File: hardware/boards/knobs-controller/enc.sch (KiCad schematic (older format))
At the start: 11 parts, among them SW1 Rotary Encoder

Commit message: 1.8 work-in-progress
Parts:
- C7, C8: footprint footprints:C0805 -> Capacitor_SMD:C_0805_2012Metric
- R10, R11, R12, R13, R14, R15, R8, R9: footprint footprints:R0805 -> Resistor_SMD:R_0805_2012Metric
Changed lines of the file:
@@
 $Descr A4 11693 8268
 encoding utf-8
-Sheet 3 13
+Sheet 5 13
 Title ""
 Date ""
@@
 AR Path="/5D86641C/5D8716A9/5D98B23E" Ref="SW3"  Part="1"
 AR Path="/5D86641C/5D87B0CB/5D98B23E" Ref="SW?"  Part="1"
-F 0 "SW1" H 5500 4570 70  0000 L BNN
+F 0 "SW3" H 5500 4570 70  0000 L BNN
 F 1 "Rotary Encoder" H 5500 3655 70  0000 L BNN
 F 2 "footprints:ENCODER_LED_3_KIT" H 6000 4150 50  0001 C CNN
@@
 AR Path="/5D86641C/5D8716A9/5D98B244" Ref="R28"  Part="1"
 AR Path="/5D86641C/5D87B0CB/5D98B244" Ref="R?"  Part="1"
-F 0 "R12" H 6850 5059 59  0000 L BNN
+F 0 "R28" H 6850 5059 59  0000 L BNN
 F 1 "10k" H 6850 4870 59  0000 L BNN
-F 2 "footprints:R0805" H 7000 5000 50  0001 C CNN
+F 2 "Resistor_SMD:R_0805_2012Metric" H 7000 5000 50  0001 C CNN
 F 3 "" H 7000 5000 50  0001 C CNN
 	1    7000 5000
@@
 AR Path="/5D86641C/5D8716A9/5D98B24A" Ref="R25"  Part="1"
 AR Path="/5D86641C/5D87B0CB/5D98B24A" Ref="R?"  Part="1"
-F 0 "R9" H 4050 3709 59  0000 L BNN
+F 0 "R25" H 4050 3709 59  0000 L BNN
 F 1 "10k" H 4050 3520 59  0000 L BNN
-F 2 "footprints:R0805" H 4200 3650 50  0001 C CNN
+F 2 "Resistor_SMD:R_0805_2012Metric" H 4200 3650 50  0001 C CNN
 F 3 "" H 4200 3650 50  0001 C CNN
 	1    4200 3650
@@
 AR Path="/5D86641C/5D8716A9/5D98B250" Ref="R24"  Part="1"
 AR Path="/5D86641C/5D87B0CB/5D98B250" Ref="R?"  Part="1"
-F 0 "R8" H 3750 4009 59  0000 L BNN
+F 0 "R24" H 3750 4009 59  0000 L BNN
 F 1 "10k" H 3750 3820 59  0000 L BNN
-F 2 "footprints:R0805" H 3900 3950 50  0001 C CNN
+F 2 "Resistor_SMD:R_0805_2012Metric" H 3900 3950 50  0001 C CNN
 F 3 "" H 3900 3950 50  0001 C CNN
 	1    3900 3950
@@
 AR Path="/5D86641C/5D8716A9/5D98B256" Ref="R27"  Part="1"
 AR Path="/5D86641C/5D87B0CB/5D98B256" Ref="R?"  Part="1"
-F 0 "R11" H 5050 3709 59  0000 L BNN
+F 0 "R27" H 5050 3709 59  0000 L BNN
 F 1 "10k" H 5050 3520 59  0000 L BNN
-F 2 "footprints:R0805" H 5200 3650 50  0001 C CNN
+F 2 "Resistor_SMD:R_0805_2012Metric" H 5200 3650 50  0001 C CNN
 F 3 "" H 5200 3650 50  0001 C CNN
 	1    5200 3650
@@
 AR Path="/5D86641C/5D8716A9/5D98B25C" Ref="R26"  Part="1"
 AR Path="/5D86641C/5D87B0CB/5D98B25C" Ref="R?"  Part="1"
-F 0 "R10" H 4750 4409 59  0000 L BNN
+F 0 "R26" H 4750 4409 59  0000 L BNN
 F 1 "10k" H 4750 4220 59  0000 L BNN
-F 2 "footprints:R0805" H 4900 4350 50  0001 C CNN
+F 2 "Resistor_SMD:R_0805_2012Metric" H 4900 4350 50  0001 C CNN
 F 3 "" H 4900 4350 50  0001 C CNN
 	1    4900 4350
@@
 AR Path="/5D86641C/5D8716A9/5D98B262" Ref="C12"  Part="1"
 AR Path="/5D86641C/5D87B0CB/5D98B262" Ref="C?"  Part="1"
-F 0 "C8" H 4660 4765 59  0000 L BNN
+F 0 "C12" H 4660 4765 59  0000 L BNN
 F 1 "10nF" H 4660 4465 59  0001 L BNN
-F 2 "footprints:C0805" H 4600 4650 50  0001 C CNN
+F 2 "Capacitor_SMD:C_0805_2012Metric" H 4600 4650 50  0001 C CNN
 F 3 "" H 4600 4650 50  0001 C CNN
 	1    4600 4650
@@
 AR Path="/5D86641C/5D8716A9/5D98B268" Ref="C11"  Part="1"
 AR Path="/5D86641C/5D87B0CB/5D98B268" Ref="C?"  Part="1"
-F 0 "C7" H 3660 4265 59  0000 L BNN
+F 0 "C11" H 3660 4265 59  0000 L BNN
 F 1 "10nF" H 3660 4065 59  0000 L BNN
-F 2 "footprints:C0805" H 3600 4250 50  0001 C CNN
+F 2 "Capacitor_SMD:C_0805_2012Metric" H 3600 4250 50  0001 C CNN
 F 3 "" H 3600 4250 50  0001 C CNN
 	1    3600 4250
@@
 AR Path="/5D86641C/5D8716A9/5D98B26E" Ref="R29"  Part="1"
 AR Path="/5D86641C/5D87B0CB/5D98B26E" Ref="R?"  Part="1"
-F 0 "R13" H 7050 3909 59  0000 L BNN
+F 0 "R29" H 7050 3909 59  0000 L BNN
 F 1 "10" H 7050 3720 59  0000 L BNN
-F 2 "footprints:R0805" H 7200 3850 50  0001 C CNN
+F 2 "Resistor_SMD:R_0805_2012Metric" H 7200 3850 50  0001 C CNN
 F 3 "" H 7200 3850 50  0001 C CNN
 	1    7200 3850
@@
 AR Path="/5D86641C/5D8716A9/5D98B274" Ref="R30"  Part="1"
 AR Path="/5D86641C/5D87B0CB/5D98B274" Ref="R?"  Part="1"
-F 0 "R14" H 7050 4209 59  0000 L BNN
+F 0 "R30" H 7050 4209 59  0000 L BNN
 F 1 "10" H 7050 4020 59  0000 L BNN
-F 2 "footprints:R0805" H 7200 4150 50  0001 C CNN
+F 2 "Resistor_SMD:R_0805_2012Metric" H 7200 4150 50  0001 C CNN
 F 3 "" H 7200 4150 50  0001 C CNN
 	1    7200 4150
@@
 AR Path="/5D86641C/5D8716A9/5D98B27A" Ref="R31"  Part="1"
 AR Path="/5D86641C/5D87B0CB/5D98B27A" Ref="R?"  Part="1"
-F 0 "R15" H 7050 4509 59  0000 L BNN
+F 0 "R31" H 7050 4509 59  0000 L BNN
 F 1 "10" H 7050 4320 59  0000 L BNN
-F 2 "footprints:R0805" H 7200 4450 50  0001 C CNN
+F 2 "Resistor_SMD:R_0805_2012Metric" H 7200 4450 50  0001 C CNN
 F 3 "" H 7200 4450 50  0001 C CNN
 	1    7200 4450
@@
 AR Path="/5D86641C/5D8716A9/5D98B281" Ref="#+3V010"  Part="1"
 AR Path="/5D86641C/5D87B0CB/5D98B281" Ref="#+3V?"  Part="1"
-F 0 "#+3V04" H 5200 3250 50  0001 C CNN
+F 0 "#+3V010" H 5200 3250 50  0001 C CNN
 F 1 "+3V3" H 5200 3372 59  0000 C CNN
 F 2 "" H 5200 3250 50  0001 C CNN
@@
 AR Path="/5D86641C/5D8716A9/5D98B287" Ref="#GND016"  Part="1"
 AR Path="/5D86641C/5D87B0CB/5D98B287" Ref="#GND?"  Part="1"
-F 0 "#GND08" H 4600 4950 50  0001 C CNN
+F 0 "#GND016" H 4600 4950 50  0001 C CNN
 F 1 "GND" H 4600 4829 59  0000 C CNN
 F 2 "" H 4600 4950 50  0001 C CNN
@@
 AR Path="/5D86641C/5D8716A9/5D98B28D" Ref="#+3V09"  Part="1"
 AR Path="/5D86641C/5D87B0CB/5D98B28D" Ref="#+3V?"  Part="1"
-F 0 "#+3V03" H 4200 3250 50  0001 C CNN
+F 0 "#+3V09" H 4200 3250 50  0001 C CNN
 F 1 "+3V3" H 4200 3372 59  0000 C CNN
 F 2 "" H 4200 3250 50  0001 C CNN
@@
 AR Path="/5D86641C/5D8716A9/5D98B293" Ref="#+3V011"  Part="1"
 AR Path="/5D86641C/5D87B0CB/5D98B293" Ref="#+3V?"  Part="1"
-F 0 "#+3V05" H 6700 3650 50  0001 C CNN
+F 0 "#+3V011" H 6700 3650 50  0001 C CNN
 F 1 "+3V3" H 6700 3772 59  0000 C CNN
 F 2 "" H 6700 3650 50  0001 C CNN
@@
 AR Path="/5D86641C/5D8716A9/5D98B299" Ref="#GND015"  Part="1"
 AR Path="/5D86641C/5D87B0CB/5D98B299" Ref="#GND?"  Part="1"
-F 0 "#GND07" H 3600 4550 50  0001 C CNN
+F 0 "#GND015" H 3600 4550 50  0001 C CNN
 F 1 "GND" H 3600 4429 59  0000 C CNN
 F 2 "" H 3600 4550 50  0001 C CNN
@@
 AR Path="/5D86641C/5D8716A9/5D98B29F" Ref="#GND018"  Part="1"
 AR Path="/5D86641C/5D87B0CB/5D98B29F" Ref="#GND?"  Part="1"
-F 0 "#GND010" H 7000 5300 50  0001 C CNN
+F 0 "#GND018" H 7000 5300 50  0001 C CNN
 F 1 "GND" H 7000 5179 59  0000 C CNN
 F 2 "" H 7000 5300 50  0001 C CNN
@@
 AR Path="/5D86641C/5D8716A9/5D98B2A5" Ref="#GND017"  Part="1"
 AR Path="/5D86641C/5D87B0CB/5D98B2A5" Ref="#GND?"  Part="1"
-F 0 "#GND09" H 5300 4550 50  0001 C CNN
+F 0 "#GND017" H 5300 4550 50  0001 C CNN
 F 1 "GND" H 5300 4429 59  0000 C CNN
 F 2 "" H 5300 4550 50  0001 C CNN

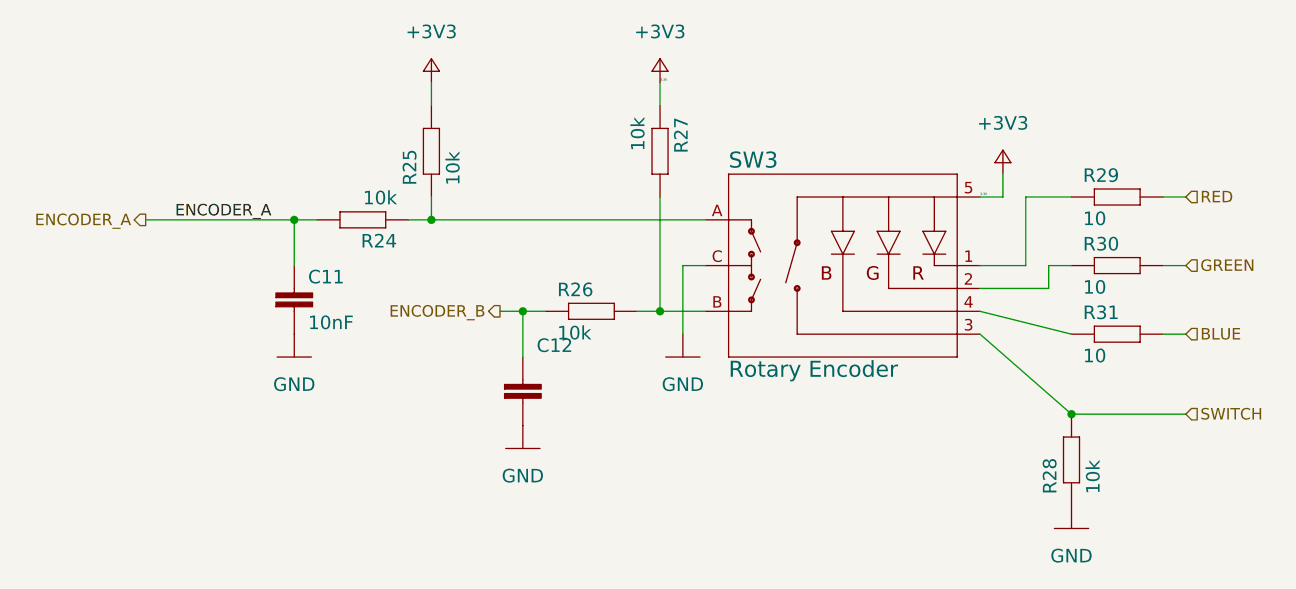
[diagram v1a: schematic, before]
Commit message: changed c6 to 0805, updates to footprints to simplify BOM
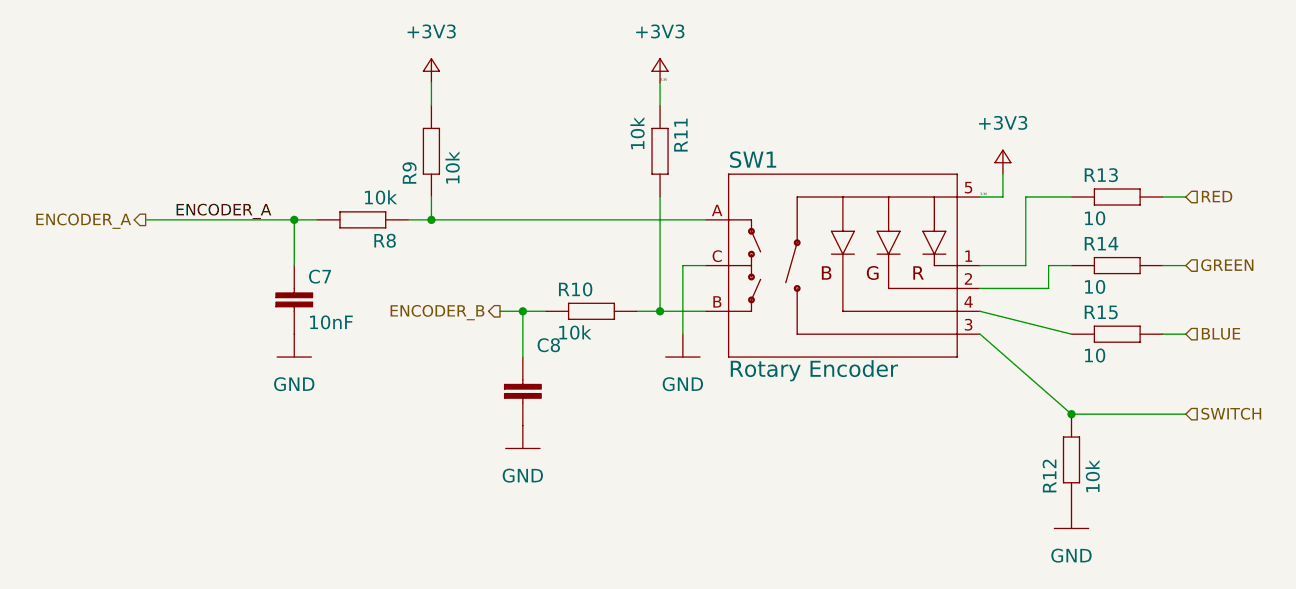
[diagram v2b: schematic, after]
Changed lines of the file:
@@
 $Descr A4 11693 8268
 encoding utf-8
-Sheet 5 13
+Sheet 3 13
 Title ""
 Date ""
@@
 AR Path="/5D86641C/5D8716A9/5D98B23E" Ref="SW3"  Part="1"
 AR Path="/5D86641C/5D87B0CB/5D98B23E" Ref="SW?"  Part="1"
-F 0 "SW3" H 5500 4570 70  0000 L BNN
+F 0 "SW1" H 5500 4570 70  0000 L BNN
 F 1 "Rotary Encoder" H 5500 3655 70  0000 L BNN
 F 2 "footprints:ENCODER_LED_3_KIT" H 6000 4150 50  0001 C CNN
@@
 AR Path="/5D86641C/5D8716A9/5D98B244" Ref="R28"  Part="1"
 AR Path="/5D86641C/5D87B0CB/5D98B244" Ref="R?"  Part="1"
-F 0 "R28" H 6850 5059 59  0000 L BNN
+F 0 "R12" H 6850 5059 59  0000 L BNN
 F 1 "10k" H 6850 4870 59  0000 L BNN
 F 2 "Resistor_SMD:R_0805_2012Metric" H 7000 5000 50  0001 C CNN
@@
 AR Path="/5D86641C/5D8716A9/5D98B24A" Ref="R25"  Part="1"
 AR Path="/5D86641C/5D87B0CB/5D98B24A" Ref="R?"  Part="1"
-F 0 "R25" H 4050 3709 59  0000 L BNN
+F 0 "R9" H 4050 3709 59  0000 L BNN
 F 1 "10k" H 4050 3520 59  0000 L BNN
 F 2 "Resistor_SMD:R_0805_2012Metric" H 4200 3650 50  0001 C CNN
@@
 AR Path="/5D86641C/5D8716A9/5D98B250" Ref="R24"  Part="1"
 AR Path="/5D86641C/5D87B0CB/5D98B250" Ref="R?"  Part="1"
-F 0 "R24" H 3750 4009 59  0000 L BNN
+F 0 "R8" H 3750 4009 59  0000 L BNN
 F 1 "10k" H 3750 3820 59  0000 L BNN
 F 2 "Resistor_SMD:R_0805_2012Metric" H 3900 3950 50  0001 C CNN
@@
 AR Path="/5D86641C/5D8716A9/5D98B256" Ref="R27"  Part="1"
 AR Path="/5D86641C/5D87B0CB/5D98B256" Ref="R?"  Part="1"
-F 0 "R27" H 5050 3709 59  0000 L BNN
+F 0 "R11" H 5050 3709 59  0000 L BNN
 F 1 "10k" H 5050 3520 59  0000 L BNN
 F 2 "Resistor_SMD:R_0805_2012Metric" H 5200 3650 50  0001 C CNN
@@
 AR Path="/5D86641C/5D8716A9/5D98B25C" Ref="R26"  Part="1"
 AR Path="/5D86641C/5D87B0CB/5D98B25C" Ref="R?"  Part="1"
-F 0 "R26" H 4750 4409 59  0000 L BNN
+F 0 "R10" H 4750 4409 59  0000 L BNN
 F 1 "10k" H 4750 4220 59  0000 L BNN
 F 2 "Resistor_SMD:R_0805_2012Metric" H 4900 4350 50  0001 C CNN
@@
 AR Path="/5D86641C/5D8716A9/5D98B262" Ref="C12"  Part="1"
 AR Path="/5D86641C/5D87B0CB/5D98B262" Ref="C?"  Part="1"
-F 0 "C12" H 4660 4765 59  0000 L BNN
+F 0 "C8" H 4660 4765 59  0000 L BNN
 F 1 "10nF" H 4660 4465 59  0001 L BNN
 F 2 "Capacitor_SMD:C_0805_2012Metric" H 4600 4650 50  0001 C CNN
@@
 AR Path="/5D86641C/5D8716A9/5D98B268" Ref="C11"  Part="1"
 AR Path="/5D86641C/5D87B0CB/5D98B268" Ref="C?"  Part="1"
-F 0 "C11" H 3660 4265 59  0000 L BNN
+F 0 "C7" H 3660 4265 59  0000 L BNN
 F 1 "10nF" H 3660 4065 59  0000 L BNN
 F 2 "Capacitor_SMD:C_0805_2012Metric" H 3600 4250 50  0001 C CNN
@@
 AR Path="/5D86641C/5D8716A9/5D98B26E" Ref="R29"  Part="1"
 AR Path="/5D86641C/5D87B0CB/5D98B26E" Ref="R?"  Part="1"
-F 0 "R29" H 7050 3909 59  0000 L BNN
+F 0 "R13" H 7050 3909 59  0000 L BNN
 F 1 "10" H 7050 3720 59  0000 L BNN
 F 2 "Resistor_SMD:R_0805_2012Metric" H 7200 3850 50  0001 C CNN
@@
 AR Path="/5D86641C/5D8716A9/5D98B274" Ref="R30"  Part="1"
 AR Path="/5D86641C/5D87B0CB/5D98B274" Ref="R?"  Part="1"
-F 0 "R30" H 7050 4209 59  0000 L BNN
+F 0 "R14" H 7050 4209 59  0000 L BNN
 F 1 "10" H 7050 4020 59  0000 L BNN
 F 2 "Resistor_SMD:R_0805_2012Metric" H 7200 4150 50  0001 C CNN
@@
 AR Path="/5D86641C/5D8716A9/5D98B27A" Ref="R31"  Part="1"
 AR Path="/5D86641C/5D87B0CB/5D98B27A" Ref="R?"  Part="1"
-F 0 "R31" H 7050 4509 59  0000 L BNN
+F 0 "R15" H 7050 4509 59  0000 L BNN
 F 1 "10" H 7050 4320 59  0000 L BNN
 F 2 "Resistor_SMD:R_0805_2012Metric" H 7200 4450 50  0001 C CNN
